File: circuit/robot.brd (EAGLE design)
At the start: 26 x 33 mm, 10 parts, among them M1 SERVO-FLIPPED, M2 SERVO-1, M3 SERVO-1, U1 ESP01

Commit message: PCBs, first proto batch
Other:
- board text added: "LEFT"
- board text added: "RIGHT"
- board text added: "WEAP"
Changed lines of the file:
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@@
 <setting verticaltext="up"/>
 </settings>
-<grid distance="1" unitdist="mm" unit="mm" style="lines" multiple="1" display="yes" altdistance="0.5" altunitdist="mm" altunit="mm"/>
+<grid distance="1" unitdist="mm" unit="mm" style="lines" multiple="1" display="yes" altdistance="0.1" altunitdist="mm" altunit="mm"/>
 <layers>
 <layer number="1" name="Top" color="4" fill="1" visible="yes" active="yes"/>
@@
 <layer number="27" name="tValues" color="7" fill="1" visible="yes" active="yes"/>
 <layer number="28" name="bValues" color="7" fill="1" visible="yes" active="yes"/>
-<layer number="29" name="tStop" color="7" fill="3" visible="no" active="yes"/>
+<layer number="29" name="tStop" color="7" fill="3" visible="yes" active="yes"/>
 <layer number="30" name="bStop" color="7" fill="6" visible="yes" active="yes"/>
 <layer number="31" name="tCream" color="7" fill="4" visible="no" active="yes"/>
@@
 <wire x1="12.9" y1="24.5" x2="12.9" y2="23.7" width="0.2032" layer="21"/>
 <text x="5.3" y="2.25" size="1.1" layer="21" font="vector" ratio="12">N</text>
-<text x="5.55" y="8.65" size="1.016" layer="25" ratio="12" rot="R90">ESP-01</text>
+<text x="7.45" y="8.75" size="1.016" layer="25" ratio="12" rot="R90">ESP-01</text>
 <text x="25.5" y="31.25" size="1.27" layer="16" ratio="12" rot="MR0">WWW.ELECCELERATOR.COM</text>
 <text x="25.5" y="31.25" size="1.27" layer="30" ratio="12" rot="MR0">WWW.ELECCELERATOR.COM</text>
@@
 <rectangle x1="8.6" y1="21.9" x2="11.5" y2="22.6" layer="42"/>
 <rectangle x1="9.3" y1="21.5" x2="11.3" y2="22.6" layer="30"/>
+<text x="0.6" y="12.4" size="1.27" layer="21" ratio="15">LEFT</text>
+<text x="25.6" y="13.6" size="1.27" layer="21" ratio="15" rot="R180">RIGHT</text>
+<text x="22" y="29.2" size="0.8128" layer="21" ratio="11" rot="R180">WEAP</text>
 </plain>
 <attributes>

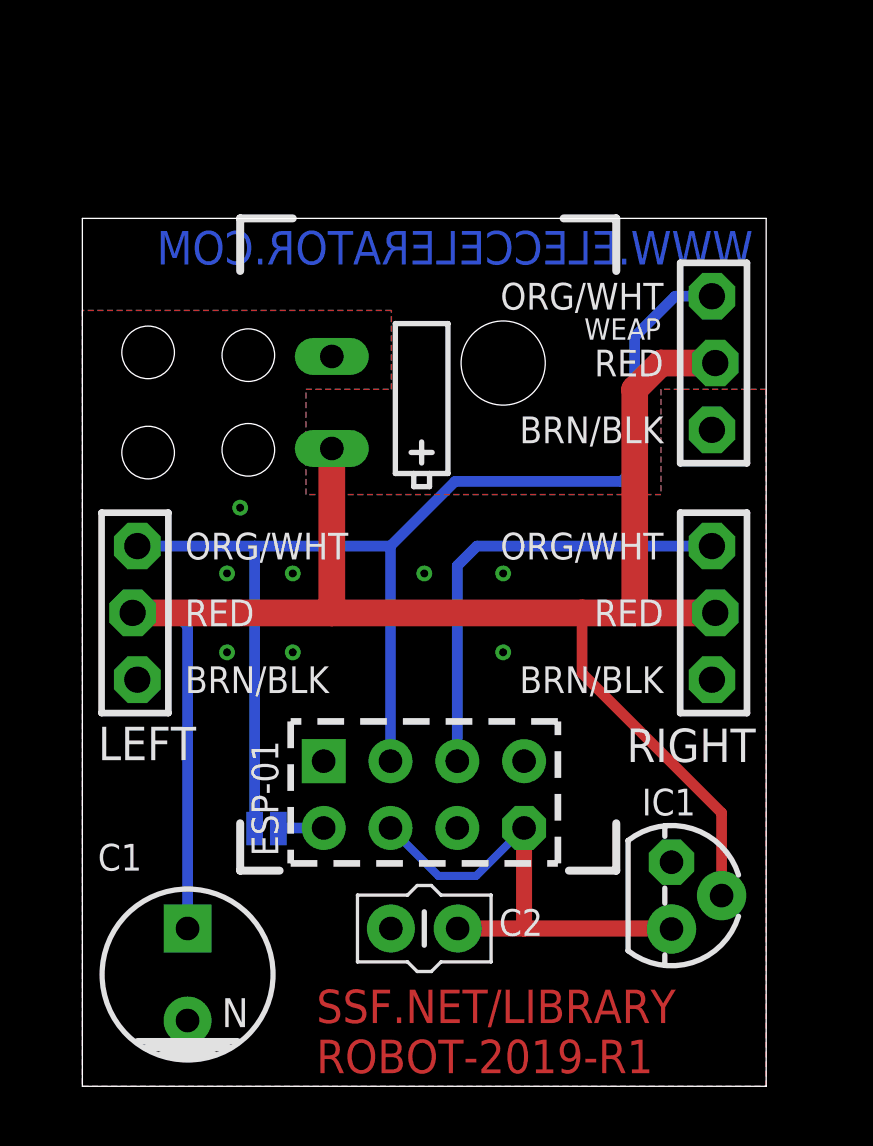
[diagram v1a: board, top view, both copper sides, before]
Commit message: second edition of the diy robot board with LM1117 vreg
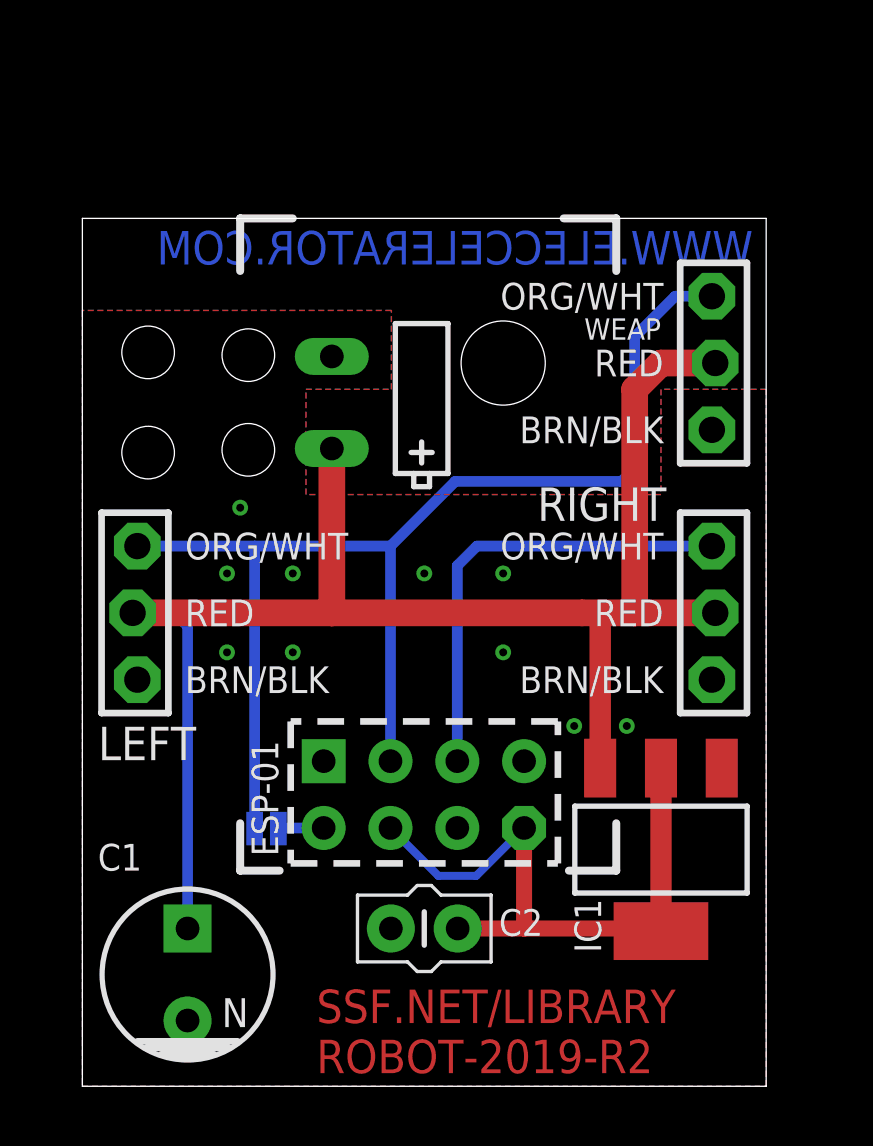
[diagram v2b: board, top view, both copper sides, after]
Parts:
- IC1: device robot:TO-92 -> robot:SOT223
- moved IC1 1.80 mm to (22.0, 9.00), turned to 180 degrees
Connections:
- net +6V: now also IC1.3; no longer IC1.2
- net 3.3V: now also IC1.2, IC1.4; no longer IC1.3
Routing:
- net +6V: track 67.1 -> 60.8 mm
- net 3.3V: track 18.6 -> 24.4 mm
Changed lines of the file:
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@@
 <rectangle x1="9.3" y1="21.5" x2="11.3" y2="22.6" layer="30"/>
 <text x="0.6" y="12.4" size="1.27" layer="21" ratio="15">LEFT</text>
-<text x="25.6" y="13.6" size="1.27" layer="21" ratio="15" rot="R180">RIGHT</text>
+<text x="17.3" y="21.5" size="1.27" layer="21" ratio="15">RIGHT</text>
 <text x="22" y="29.2" size="0.8128" layer="21" ratio="11" rot="R180">WEAP</text>
 </plain>
@@
 <element name="U$9" library="robot" package="TEXT-INFO-MINI" value="TEXT-INFO-MINI" x="8.9" y="0.5"/>
 <element name="U1" library="robot" package="ESP01" value="ESP01" x="13" y="18"/>
-<element name="IC1" library="robot" package="TO-92" value="" x="22.4" y="7.25" smashed="yes" rot="R270">
-<attribute name="NAME" x="21.273259375" y="10.298490625" size="1.016" layer="25" ratio="10"/>
-<attribute name="VALUE" x="21.13" y="4.075" size="0.4064" layer="27" ratio="10" rot="R270"/>
-</element>
 <element name="C1" library="robot" package="CPOL-RADIAL-100UF-25V" value="" x="4" y="4.25" smashed="yes" rot="R90">
 <attribute name="VALUE" x="8.318" y="2.345" size="0.8128" layer="27" rot="R90"/>
@@
 <element name="SJ1" library="robot" package="SJ_2S-NO" value="" x="7" y="9.8" smashed="yes" rot="MR180">
 <attribute name="VALUE" x="6.092" y="11.451" size="0.4064" layer="28" rot="MR180"/>
+</element>
+<element name="IC1" library="robot" package="SOT223" value="" x="22" y="9" smashed="yes" rot="R180">
+<attribute name="NAME" x="18.7085" y="7.1255" size="1.016" layer="25" font="vector" rot="R270"/>
+<attribute name="VALUE" x="23.0795" y="9.1905" size="0.4064" layer="27" rot="R180"/>
 </element>
 </elements>
@@
 <contactref element="BATTERY" pad="NEG"/>
 <contactref element="C2" pad="2"/>
-<contactref element="IC1" pad="1"/>
 <contactref element="C1" pad="2"/>
 <contactref element="U1" pad="GND"/>
@@
 <via x="5.5" y="16.5" extent="1-16" drill="0.3" shape="octagon"/>
 <via x="13" y="19.5" extent="1-16" drill="0.3" shape="octagon"/>
+<contactref element="IC1" pad="1"/>
+<via x="18.7" y="13.7" extent="1-16" drill="0.3" shape="octagon"/>
+<via x="20.7" y="13.7" extent="1-16" drill="0.3" shape="octagon"/>
 </signal>
 <signal name="SERVO-RIGHT">
@@
 <contactref element="M1" pad="PWR"/>
 <contactref element="C1" pad="1"/>
-<contactref element="IC1" pad="2"/>
 <wire x1="9.485" y1="24.25" x2="9.485" y2="18" width="1.016" layer="1"/>
 <wire x1="9.485" y1="18" x2="1.9111" y2="18" width="1.016" layer="1"/>
@@
 <wire x1="21" y1="18" x2="19" y2="18" width="1.016" layer="1"/>
 <wire x1="19" y1="18" x2="9.485" y2="18" width="1.016" layer="1"/>
-<wire x1="24.305" y1="7.25" x2="24.305" y2="10.395" width="0.4064" layer="1"/>
 <wire x1="4" y1="6" x2="4" y2="17.5" width="0.4064" layer="16"/>
 <wire x1="4" y1="17.5" x2="3.5" y2="18" width="0.4064" layer="16"/>
@@
 <wire x1="22" y1="27.5" x2="21" y2="26.5" width="1.016" layer="1"/>
 <wire x1="21" y1="26.5" x2="21" y2="18" width="1.016" layer="1"/>
-<wire x1="24.305" y1="10.395" x2="19" y2="15.7" width="0.4064" layer="1"/>
-<wire x1="19" y1="15.7" x2="19" y2="18" width="0.4064" layer="1"/>
+<contactref element="IC1" pad="3"/>
+<wire x1="19.6886" y1="12.0988" x2="19.6886" y2="18" width="0.8128" layer="1"/>
+<wire x1="19.6886" y1="18" x2="19" y2="18" width="0.8128" layer="1"/>
 </signal>
 <signal name="3.3V">
 <contactref element="C2" pad="1"/>
-<contactref element="IC1" pad="3"/>
 <contactref element="U1" pad="VCC"/>
 <wire x1="16.795" y1="9.8225" x2="16.795" y2="6" width="0.6096" layer="1"/>
 <wire x1="14.27" y1="6" x2="16.795" y2="6" width="0.6096" layer="1"/>
-<wire x1="22.4" y1="5.98" x2="22.38" y2="6" width="0.6096" layer="1"/>
-<wire x1="22.38" y1="6" x2="16.795" y2="6" width="0.6096" layer="1"/>
 <contactref element="U1" pad="CH_PD"/>
 <wire x1="16.795" y1="9.8225" x2="14.9725" y2="8" width="0.3048" layer="16"/>
 <wire x1="14.9725" y1="8" x2="13.5375" y2="8" width="0.3048" layer="16"/>
 <wire x1="13.5375" y1="8" x2="11.715" y2="9.8225" width="0.3048" layer="16"/>
+<contactref element="IC1" pad="2"/>
+<contactref element="IC1" pad="4"/>
+<wire x1="22" y1="12.0988" x2="22" y2="5.901" width="0.8128" layer="1"/>
+<wire x1="16.795" y1="6" x2="22" y2="6" width="0.6096" layer="1"/>
+<wire x1="22" y1="6" x2="22" y2="5.901" width="0.6096" layer="1"/>
 </signal>
 <signal name="N$1">

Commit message: added Wemos based PCB
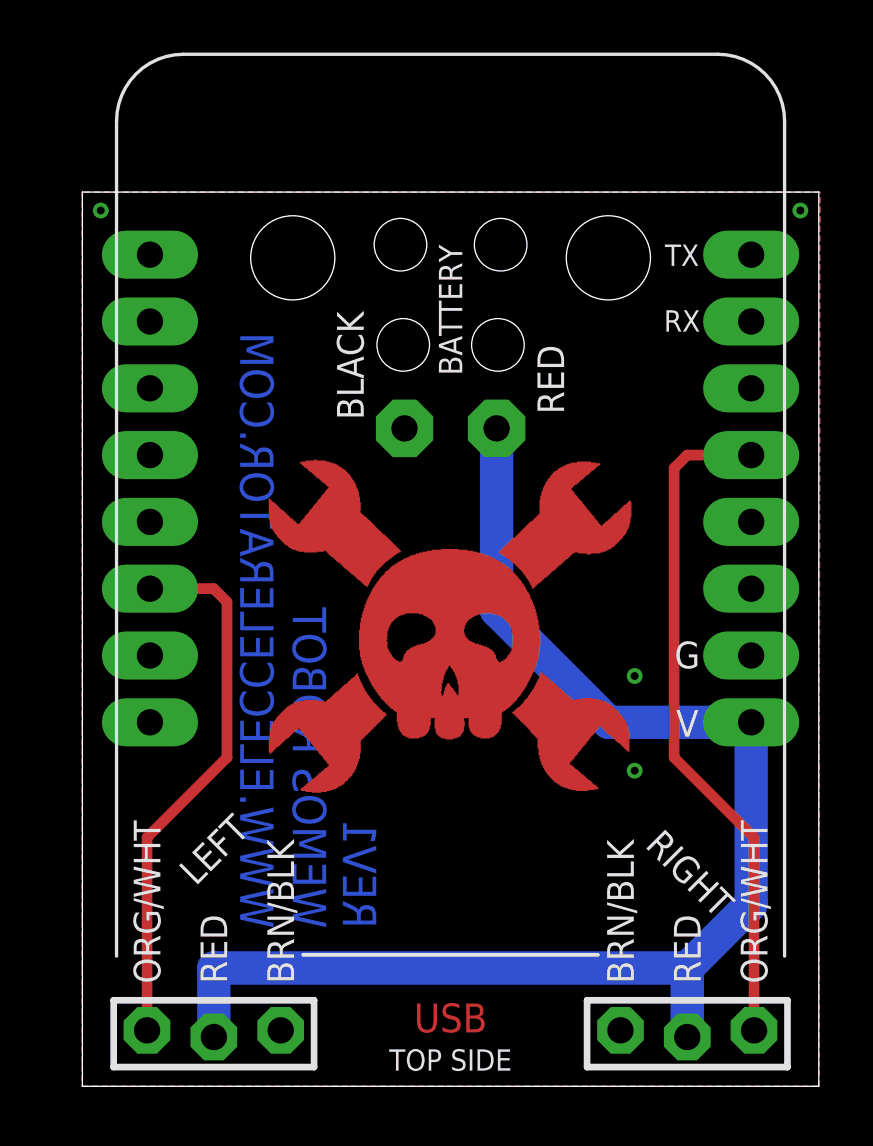
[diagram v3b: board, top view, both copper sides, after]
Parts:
- removed C1: (no value), robot:CPOL-RADIAL-100UF-25V
- removed C2: (no value), robot:CAP-PTH-SMALL
- removed IC1: (no value), robot:SOT223
- removed M3: SERVO-1, robot:SERVO
- removed SJ1: (no value), robot:SJ_2S-NO
- removed U1: ESP01, robot:ESP01
- added U$1: HACKADAY-14MM, robot:HACKADAY-1
- added WEMOS1: (no value), robot:WEMOS-D1-MINI
- moved M1 16.3 mm to (5.00, 2.00), turned to 0 degrees
- moved M2 16.0 mm to (23.0, 2.00), turned to 0 degrees
- moved BATTERY 13.0 mm to (14.0, 32.0), flipped to the bottom, turned to 90 degrees
- moved U$9 5.57 mm to (8.00, 6.00), flipped to the bottom, turned to 90 degrees
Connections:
- removed net 3.3V: C2.1, IC1.2, IC1.4, U1.CH_PD, U1.VCC
- removed net N$1: SJ1.2, U1.TX
- net +6V: now also WEMOS1.5V; no longer C1.1, IC1.3, M3.PWR
- net GND: now also WEMOS1.GND; no longer C1.2, C2.2, IC1.1, M3.GND, U1.GND
- net SERVO-LEFT: now also WEMOS1.D7; no longer M3.SIG, SJ1.1, U1.GPIO2
- net SERVO-RIGHT: now also WEMOS1.D2; no longer U1.GPIO0
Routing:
- net SERVO-LEFT: track 47.6 -> 20.7 mm
- net 3.3V: track 24.4 -> 0.00 mm
- net +6V: track 60.8 -> 52.0 mm
- net SERVO-RIGHT: track 17.4 -> 25.8 mm
- net N$1: track 1.75 -> 0.00 mm
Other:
- board size 26 x 33 mm -> 28 x 34 mm
- board text added: "BOTTOM SIDE"
- board text added: "G"
- board text added: "RX"
- board text added: "TOP SIDE"
- board text added: "TX"
- board text added: "USB"
- board text added: "V"
- board text removed: "ESP-01"
- board text removed: "N"
- board text removed: "WEAP"
